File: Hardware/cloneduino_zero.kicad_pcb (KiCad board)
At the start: 4 copper layers, 50 x 19.6 mm, 34 parts, among them J1 USB-C Receptacle, J2 MicroSD Slot, J3 Conn_01x20, J4 Conn_01x20, J5 Conn_01x04, SW1 SW_Push, U1 SPX3819M5-L-3-3, U2 ATSAMD21G18A-A, Y1 32kHz

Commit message: Fix bottom silkscreen references
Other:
- board text added: "D27"
- board text added: "PA30 D44"
- board text added: "PA31 D45"
- board text removed: "PA30 SWCLK"
- board text removed: "PA31 SWDIO"

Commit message: Rename reset switch
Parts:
- J5: value Conn_01x04 -> SWD
- SW1: value SW_Push -> Reset Switch

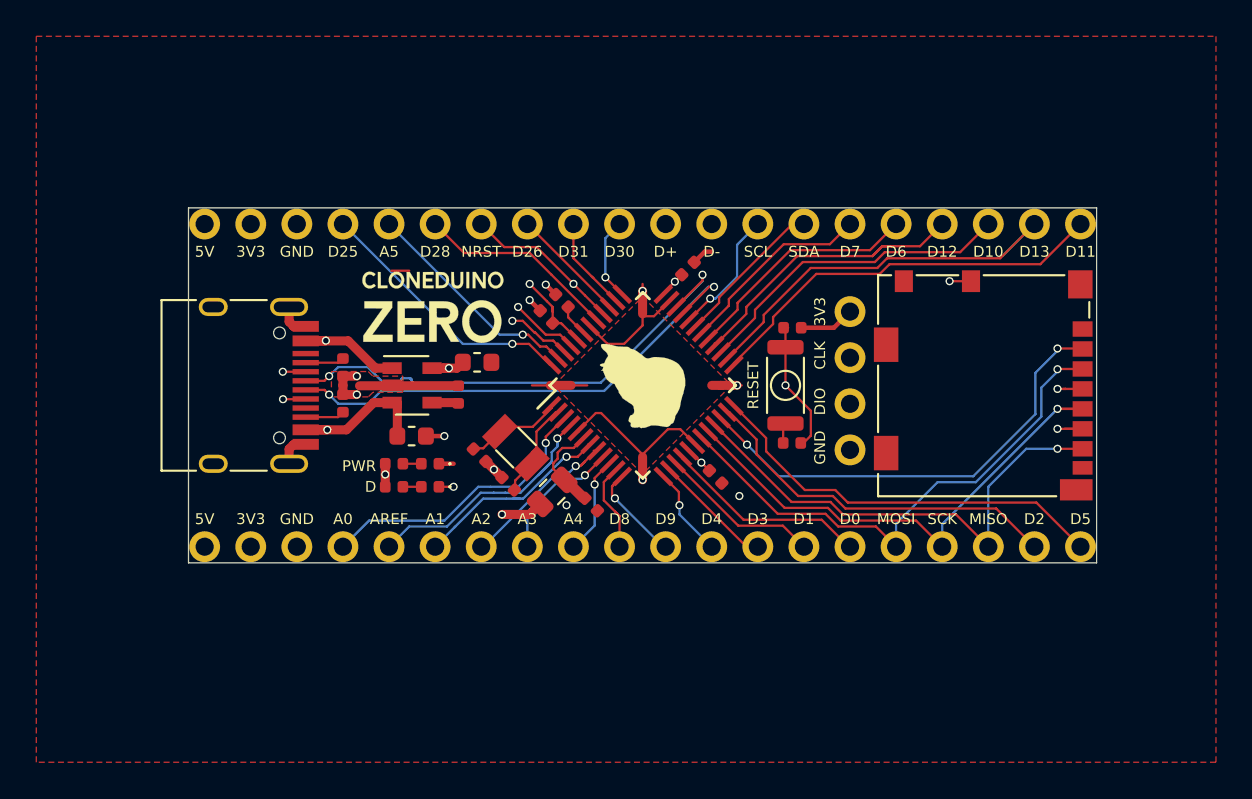
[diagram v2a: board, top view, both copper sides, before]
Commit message: Keep PCB width under 50 mm
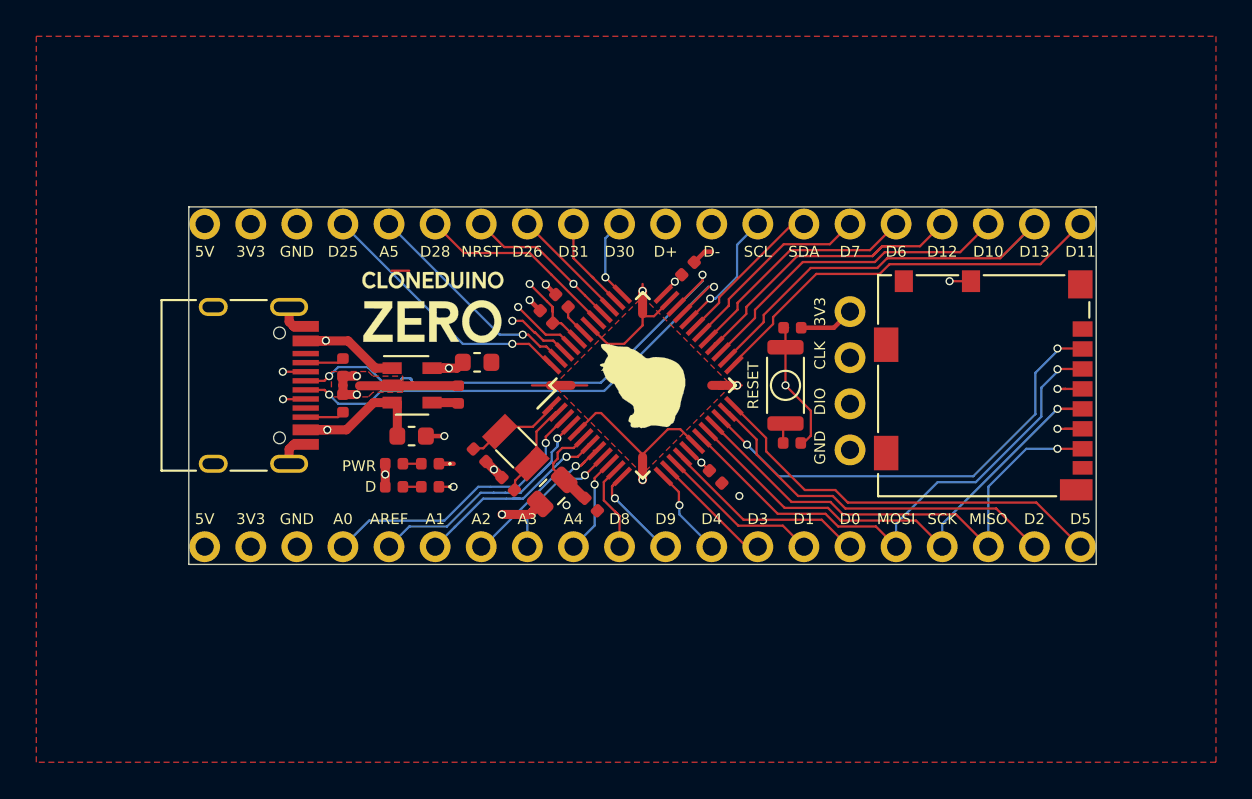
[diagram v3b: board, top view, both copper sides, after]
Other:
- board size 50 x 19.6 mm -> 50 x 19.7 mm

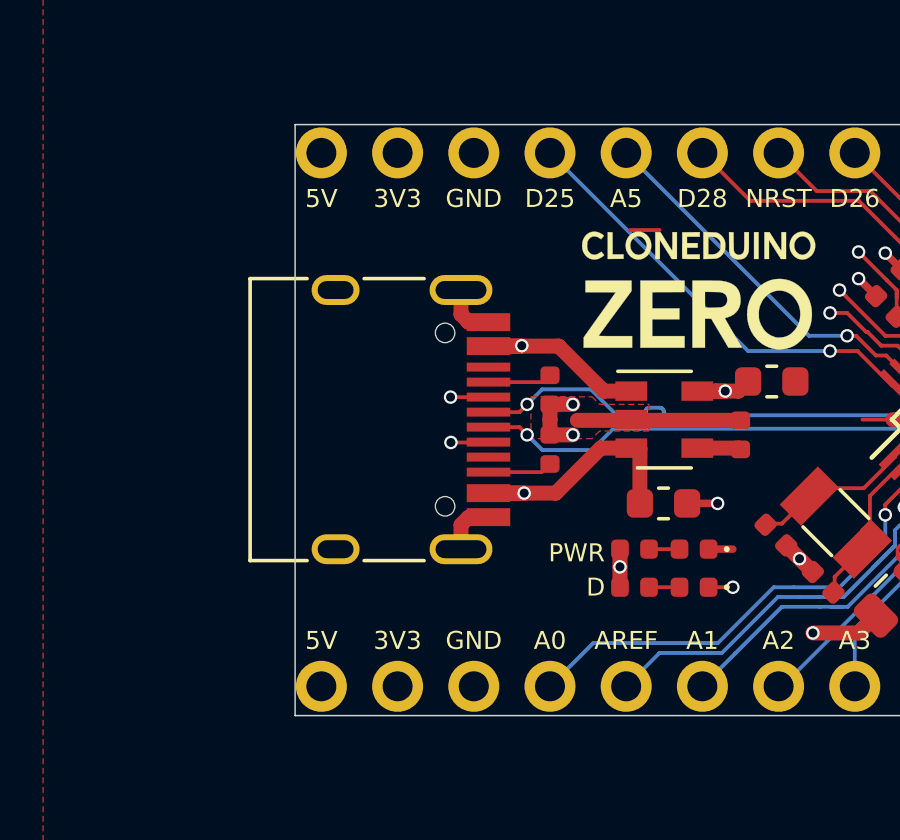
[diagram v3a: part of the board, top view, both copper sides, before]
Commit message: Change silkscreen markings
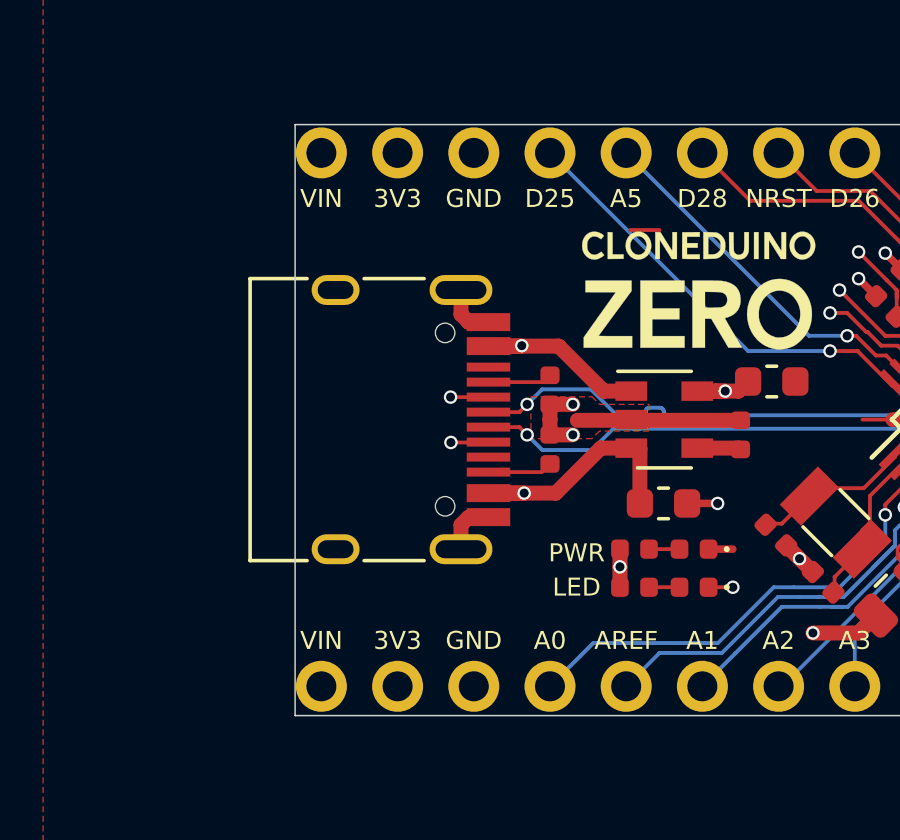
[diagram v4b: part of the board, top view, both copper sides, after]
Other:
- board text added: "LED"
- board text added: "VIN"
- board text removed: "5V"
- board text removed: "D"
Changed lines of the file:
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@@
     (effects (font (size 0.6 0.6) (thickness 0.1)) (justify mirror))
   )
-  (gr_text 5V (at 49.276 86.868) (layer B.SilkS)
+  (gr_text VIN (at 49.276 86.868) (layer B.SilkS)
     (effects (font (size 0.6 0.6) (thickness 0.1)) (justify mirror))
   )
@@
     (effects (font (size 0.6 0.6) (thickness 0.1)) (justify mirror))
   )
-  (gr_text 5V (at 49.276 101.6) (layer F.SilkS)
+  (gr_text VIN (at 49.276 101.6) (layer F.SilkS)
     (effects (font (size 0.6 0.6) (thickness 0.1)))
   )
@@
     (effects (font (size 0.6 0.6) (thickness 0.1)) (justify mirror))
   )
-  (gr_text D (at 58.42 99.822) (layer F.SilkS)
+  (gr_text LED (at 57.785 99.822) (layer F.SilkS)
     (effects (font (size 0.6 0.6) (thickness 0.1)))
   )
@@
     (effects (font (size 0.6 0.6) (thickness 0.1)))
   )
-  (gr_text 5V (at 49.276 101.6) (layer B.SilkS)
+  (gr_text VIN (at 49.276 101.6) (layer B.SilkS)
     (effects (font (size 0.6 0.6) (thickness 0.1)) (justify mirror))
   )
@@
     (effects (font (size 0.6 0.6) (thickness 0.1)))
   )
-  (gr_text 5V (at 49.276 86.868) (layer F.SilkS)
-    (effects (font (size 0.6 0.6) (thickness 0.1)))
-  )
+  (gr_text VIN (at 49.276 86.868) (layer F.SilkS)
+    (effects (font (size 0.6 0.6) (thickness 0.1)))
+  )

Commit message: Add solder points
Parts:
- added J6: Conn_01x20, Connector_PinHeader_2.54mm:PinHeader_1x20_P2.54mm_Vertical, F.Cu at (49.3, 105.4)
- added J7: Conn_01x20, Connector_PinHeader_2.54mm:PinHeader_1x20_P2.54mm_Vertical, F.Cu at (97.5, 83.1)
- C6: value 2.2u -> 4.7u
- R1, R2: value 4k7 -> 5k1
- R5: value 10k -> 5k1
- Y1: value 32kHz -> 32.768kHz
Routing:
- net +5V: track 15.2 -> 22.5 mm
- net GND: track 50.6 -> 57.9 mm
- net +3V3: track 21.8 -> 29.1 mm
- net /PA17: track 69.5 -> 73.2 mm
- net /PA20: track 13.2 -> 16.9 mm
- net /PB22: track 4.59 -> 8.27 mm
- net /USB_D+: track 35.8 -> 39.5 mm
- net /PB23: track 5.29 -> 8.97 mm
- net /PB03: track 14.6 -> 18.3 mm
- net /PB02: track 12.4 -> 16.1 mm
- net /PA28: track 11.1 -> 14.8 mm
- net /PA23: track 7.02 -> 10.7 mm
- net /PA22: track 8.49 -> 12.2 mm
- net /PA21: track 10.9 -> 14.5 mm
- net /PA19: track 17.1 -> 20.8 mm
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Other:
- board size 50 x 19.7 mm -> 50 x 22.3 mm
